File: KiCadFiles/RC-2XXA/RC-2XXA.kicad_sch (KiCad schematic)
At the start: 252 parts, among them J1 Conn_01x01_Pin, J2 Conn_01x04_Pin, J3 Conn_01x04_Pin, J4 Conn_01x07_Socket, J5 Conn_01x07_Socket, SW1 SW_DPST_x2, SW2 SW_DPST_x2, U1 TLV74318PDBVR, U2 PMW3360DM-T2QU, U3 TPD4E05U06DQAR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

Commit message: Add Solder Jumper component and associated wiring to RC-2XXA schematic
- Introduced a new Solder Jumper component (JP) with properties including reference, value, footprint, and description.
- Added multiple instances of the Solder Jumper at specified coordinates in the schematic.
- Updated wiring to accommodate the new component, ensuring proper connections.
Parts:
- added JP1, JP2, JP3: SolderJumper_2_Open, Jumper:SolderJumper-2_P1.3mm_Open_RoundedPad1.0x1.5mm, symbol Jumper:SolderJumper_2_Open
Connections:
- net CAPLED: now also JP2.1 (A); no longer R7.2
- net NUMLED: now also JP3.1 (A); no longer R9.2
- net SCLLED: now also JP1.1 (A); no longer R3.2
- new net: JP2.2 (B), R7.2
- new net: JP1.2 (B), R3.2
- new net: JP3.2 (B), R9.2
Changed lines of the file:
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@@
 	(wire
 		(pts
+			(xy 328.93 340.36) (xy 331.47 340.36)
+		)
+		(stroke
+			(width 0)
+			(type default)
+		)
+	)
+	(wire
+		(pts
 			(xy 204.47 24.13) (xy 204.47 34.29)
 		)
@@
 	(wire
 		(pts
+			(xy 328.93 370.84) (xy 331.47 370.84)
+		)
+		(stroke
+			(width 0)
+			(type default)
+		)
+	)
+	(wire
+		(pts
 			(xy 320.04 327.66) (xy 331.47 327.66)
 		)
@@
 	(wire
 		(pts
-			(xy 320.04 340.36) (xy 331.47 340.36)
+			(xy 320.04 340.36) (xy 321.31 340.36)
 		)
 		(stroke
@@
 	(wire
 		(pts
-			(xy 320.04 309.88) (xy 331.47 309.88)
+			(xy 320.04 309.88) (xy 322.58 309.88)
 		)
 		(stroke
@@
 	(wire
 		(pts
+			(xy 330.2 309.88) (xy 331.47 309.88)
+		)
+		(stroke
+			(width 0)
+			(type default)
+		)
+	)
+	(wire
+		(pts
 			(xy 351.79 107.95) (xy 361.95 107.95)
 		)
@@
 	(wire
 		(pts
-			(xy 320.04 370.84) (xy 331.47 370.84)
+			(xy 320.04 370.84) (xy 321.31 370.84)
 		)
 		(stroke
@@
 	)
 	(symbol
+		(lib_id "Jumper:SolderJumper_2_Open")
+		(at 326.39 309.88 0)
+		(unit 1)
+		(exclude_from_sim no)
+		(in_bom no)
+		(on_board yes)
+		(dnp no)
+		(property "Reference" "JP1"
+			(at 337.058 308.356 0)
+			(effects
+				(font
+					(size 1.27 1.27)
+				)
+			)
+		)
+		(property "Value" "SolderJumper_2_Open"
+			(at 326.39 306.07 0)
+			(effects
+				(font
+					(size 1.27 1.27)
+				)
+			)
+		)
+		(property "Footprint" "Jumper:SolderJumper-2_P1.3mm_Open_RoundedPad1.0x1.5mm"
+			(at 326.39 309.88 0)
+			(effects
+				(font
+					(size 1.27 1.27)
+				)
+				(hide yes)
+			)
+		)
+		(property "Datasheet" "~"
+			(at 326.39 309.88 0)
+			(effects
+				(font
+					(size 1.27 1.27)
+				)
+				(hide yes)
+			)
+		)
+		(property "Description" "Solder Jumper, 2-pole, open"
+			(at 326.39 309.88 0)
+			(effects
+				(font
+					(size 1.27 1.27)
+				)
+				(hide yes)
+			)
+		)
+		(pin "1"
+		)
+		(pin "2"
+		)
+		(instances
+			(project "RC-2XXA"
+				(path "/65196bbe-5350-405f-9fe2-667d33111e14"
+					(reference "JP1")
+					(unit 1)
+				)
+			)
+		)
+	)
+	(symbol
 		(lib_id "Device:D")
 		(at 487.68 66.04 90)
@@
 	)
 	(symbol
+		(lib_id "Jumper:SolderJumper_2_Open")
+		(at 325.12 370.84 0)
+		(unit 1)
+		(exclude_from_sim no)
+		(in_bom no)
+		(on_board yes)
+		(dnp no)
+		(property "Reference" "JP3"
+			(at 337.058 369.316 0)
+			(effects
+				(font
+					(size 1.27 1.27)
+				)
+			)
+		)
+		(property "Value" "SolderJumper_2_Open"
+			(at 325.12 367.03 0)
+			(effects
+				(font
+					(size 1.27 1.27)
+				)
+			)
+		)
+		(property "Footprint" "Jumper:SolderJumper-2_P1.3mm_Open_RoundedPad1.0x1.5mm"
+			(at 325.12 370.84 0)
+			(effects
+				(font
+					(size 1.27 1.27)
+				)
+				(hide yes)
+			)
+		)
+		(property "Datasheet" "~"
+			(at 325.12 370.84 0)
+			(effects
+				(font
+					(size 1.27 1.27)
+				)
+				(hide yes)
+			)
+		)
+		(property "Description" "Solder Jumper, 2-pole, open"
+			(at 325.12 370.84 0)
+			(effects
+				(font
+					(size 1.27 1.27)
+				)
+				(hide yes)
+			)
+		)
+		(pin "1"
+		)
+		(pin "2"
+		)
+		(instances
+			(project "RC-2XXA"
+				(path "/65196bbe-5350-405f-9fe2-667d33111e14"
+					(reference "JP3")
+					(unit 1)
+				)
+			)
+		)
+	)
+	(symbol
 		(lib_id "Device:C")
 		(at 149.86 388.62 0)
@@
 					(unit 1)
 				)
+			)
+		)
+	)
+	(symbol
+		(lib_id "Jumper:SolderJumper_2_Open")
+		(at 325.12 340.36 0)
+		(unit 1)
+		(exclude_from_sim no)
+		(in_bom no)
+		(on_board yes)
+		(dnp no)
+		(property "Reference" "JP2"
+			(at 337.058 338.836 0)
+			(effects
+				(font
+					(size 1.27 1.27)
+				)
+			)
+		)
+		(property "Value" "SolderJumper_2_Open"
+			(at 325.12 336.55 0)
+			(effects
+				(font
+					(size 1.27 1.27)
+				)
+			)
+		)
+		(property "Footprint" "Jumper:SolderJumper-2_P1.3mm_Open_RoundedPad1.0x1.5mm"
+			(at 325.12 340.36 0)
+			(effects
+				(font
+					(size 1.27 1.27)
+				)
+				(hide yes)
+			)
+		)
+		(property "Datasheet" "~"
+			(at 325.12 340.36 0)
+			(effects
+				(font
+					(size 1.27 1.27)
+				)
+				(hide yes)
+			)
+		)
+		(property "Description" "Solder Jumper, 2-pole, open"
+			(at 325.12 340.36 0)
+			(effects
+				(font
+					(size 1.27 1.27)
+				)
+				(hide yes)
+			)
+		)
+		(pin "1"
+		)
+		(pin "2"
+		)
+		(instances
+			(project "RC-2XXA"
+				(path "/65196bbe-5350-405f-9fe2-667d33111e14"
+					(reference "JP2")
+					(unit 1)
+				)

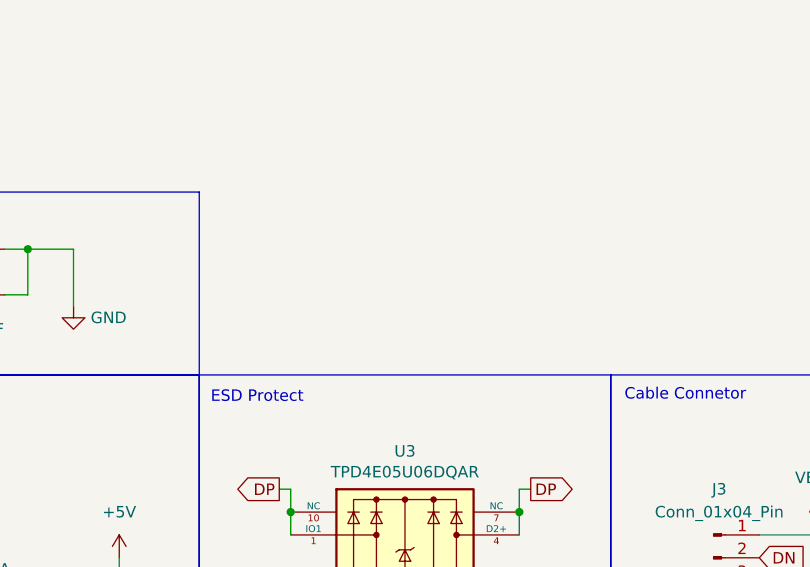
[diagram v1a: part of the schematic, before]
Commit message: Add Mounting Hole Pad and GND symbol to schematic
- Introduced a new symbol for a mounting hole pad with properties including reference, value, footprint, and description.
- Added a graphical representation of the mounting hole pad with a circle.
- Included a GND symbol with properties for reference, value, and description, creating a global label for ground.
- Updated the schematic layout to accommodate the new components.
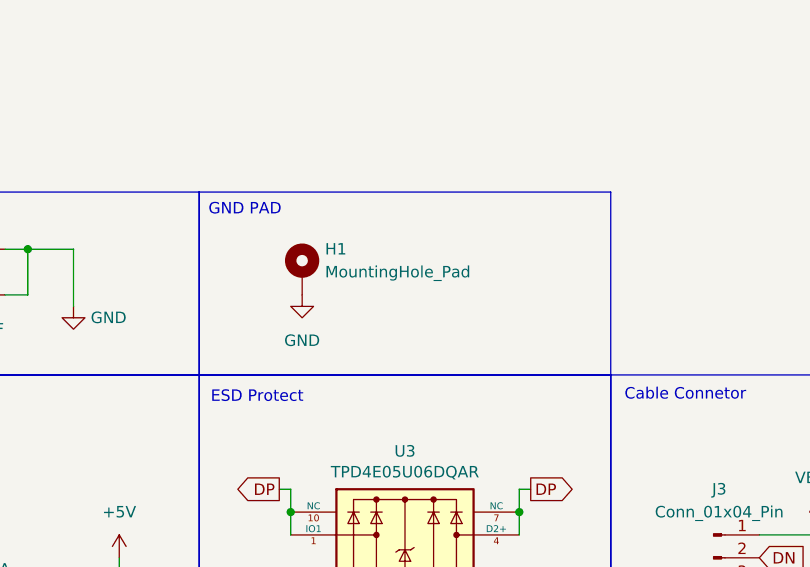
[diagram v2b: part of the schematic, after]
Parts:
- added H1: MountingHole_Pad, My-Fi Footprints:Cherry-GND-PAD, symbol Mechanical:MountingHole_Pad
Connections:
- net GND: now also H1.1
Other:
- note added: "GND PAD"
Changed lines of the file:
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@@
 	)
 	(rectangle
+		(start 176.53 303.53)
+		(end 222.25 323.85)
+		(stroke
+			(width 0)
+			(type default)
+		)
+		(fill
+			(type none)
+		)
+	)
+	(rectangle
 		(start 127 303.53)
 		(end 176.53 323.85)
@@
 		)
 	)
+	(text "GND PAD"
+		(exclude_from_sim no)
+		(at 177.546 305.562 0)
+		(effects
+			(font
+				(size 1.27 1.27)
+			)
+			(justify left)
+		)
+	)
 	(junction
 		(at 204.47 102.87)
@@
 	)
 	(symbol
+		(lib_id "Mechanical:MountingHole_Pad")
+		(at 187.96 312.42 0)
+		(unit 1)
+		(exclude_from_sim no)
+		(in_bom no)
+		(on_board yes)
+		(dnp no)
+		(fields_autoplaced yes)
+		(property "Reference" "H1"
+			(at 190.5 309.8799 0)
+			(effects
+				(font
+					(size 1.27 1.27)
+				)
+				(justify left)
+			)
+		)
+		(property "Value" "MountingHole_Pad"
+			(at 190.5 312.4199 0)
+			(effects
+				(font
+					(size 1.27 1.27)
+				)
+				(justify left)
+			)
+		)
+		(property "Footprint" "My-Fi Footprints:Cherry-GND-PAD"
+			(at 187.96 312.42 0)
+			(effects
+				(font
+					(size 1.27 1.27)
+				)
+				(hide yes)
+			)
+		)
+		(property "Datasheet" "~"
+			(at 187.96 312.42 0)
+			(effects
+				(font
+					(size 1.27 1.27)
+				)
+				(hide yes)
+			)
+		)
+		(property "Description" "Mounting Hole with connection"
+			(at 187.96 312.42 0)
+			(effects
+				(font
+					(size 1.27 1.27)
+				)
+				(hide yes)
+			)
+		)
+		(pin "1"
+		)
+		(instances
+			(project ""
+				(path "/65196bbe-5350-405f-9fe2-667d33111e14"
+					(reference "H1")
+					(unit 1)
+				)
+			)
+		)
+	)
+	(symbol
 		(lib_id "Regulator_Linear:XC6206PxxxMR")
 		(at 232.41 384.81 0)
@@
 					(unit 1)
 				)
+			)
+		)
+	)
+	(symbol
+		(lib_id "power:GND")
+		(at 187.96 314.96 0)
+		(unit 1)
+		(exclude_from_sim no)
+		(in_bom yes)
+		(on_board yes)
+		(dnp no)
+		(fields_autoplaced yes)
+		(property "Reference" "#PWR014"
+			(at 187.96 321.31 0)
+			(effects
+				(font
+					(size 1.27 1.27)
+				)
+				(hide yes)
+			)
+		)
+		(property "Value" "GND"
+			(at 187.96 320.04 0)
+			(effects
+				(font
+					(size 1.27 1.27)
+				)
+			)
+		)
+		(property "Footprint" ""
+			(at 187.96 314.96 0)
+			(effects
+				(font
+					(size 1.27 1.27)
+				)
+				(hide yes)
+			)
+		)
+		(property "Datasheet" ""
+			(at 187.96 314.96 0)
+			(effects
+				(font
+					(size 1.27 1.27)
+				)
+				(hide yes)
+			)
+		)
+		(property "Description" "Power symbol creates a global label with name \"GND\" , ground"
+			(at 187.96 314.96 0)
+			(effects
+				(font
+					(size 1.27 1.27)
+				)
+				(hide yes)
+			)
+		)
+		(pin "1"
+		)
+		(instances
+			(project "RC-2XXA"
+				(path "/65196bbe-5350-405f-9fe2-667d33111e14"
+					(reference "#PWR014")
+					(unit 1)
+				)

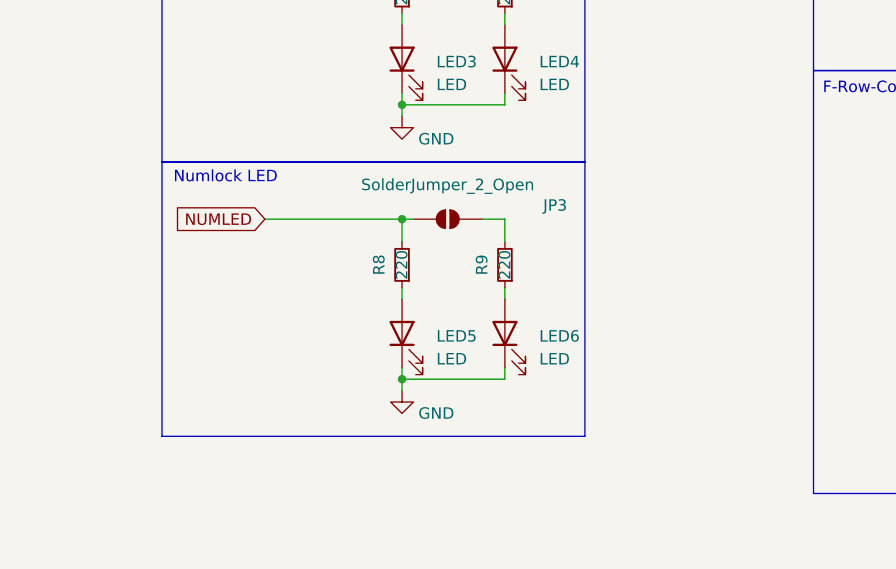
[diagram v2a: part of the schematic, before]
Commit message: Add Solder Jumper and update component positions in schematic
- Introduced a new Solder Jumper component (JP4) with properties and graphical representation.
- Adjusted positions of several components including resistors (R8, R9, R11) and LEDs (LED6, LED7) for better layout.
- Updated junctions and wire connections to reflect new component placements.
- Removed redundant junctions and wires to clean up the schematic.
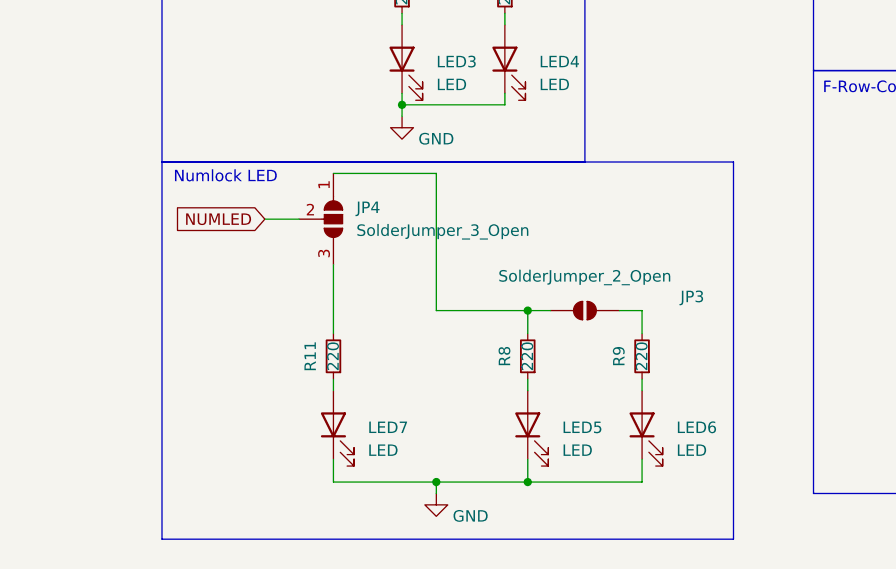
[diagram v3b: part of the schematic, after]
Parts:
- added JP4: SolderJumper_3_Open, Jumper:SolderJumper-3_P1.3mm_Open_RoundedPad1.0x1.5mm, symbol Jumper:SolderJumper_3_Open
- added LED7: LED, My-Fi Footprints:DIP_LED_MX_3mm, symbol Device:LED
- added R11: 220, Resistor_SMD:R_0805_2012Metric_Pad1.20x1.40mm_HandSolder, symbol Device:R_Small
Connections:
- net GND: now also LED7.1 (K)
- net NUMLED: now also JP4.2 (C); no longer JP3.1 (A), R8.2
- new net: JP3.1 (A), JP4.1 (A), R8.2
- new net: JP4.3 (B), R11.2
- new net: LED7.2 (A), R11.1
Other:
- moved on the sheet: JP3, LED5, LED6, R8, R9

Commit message: Refactor code structure for improved readability and maintainability
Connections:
- net COL0: now also U4.43 (PB7)
- net COL1: now also U4.42 (PB6)
- net COL10: now also U4.28 (PB15)
- net COL11: now also U4.27 (PB14)
- net COL12: now also U4.26 (PB13)
- net COL13: now also U4.25 (PB12)
- net COL14: now also U4.22 (PB11)
- net COL15: now also U4.21 (PB10)
- net COL16: now also U4.20 (PB2)
- net COL17: now also U4.5 (PF0)
- net COL18: now also U4.4 (PC15)
- net COL19: now also U4.3 (PC14)
- net COL2: now also U4.40 (PB4)
- net COL20: now also U4.2 (PC13)
- net COL3: now also U4.39 (PB3)
- net COL4: now also U4.38 (PA15)
- net COL5: now also U4.37 (PA14)
- net COL6: now also U4.34 (PA13)
- net COL7: now also U4.31 (PA10)
- net COL8: now also U4.30 (PA9)
- net COL9: now also U4.29 (PA8)
- net NUMLED: now also JP3.1 (A)
- net ROW0: now also U4.45 (PB8)
- net ROW1: now also U4.46 (PB9)
- net ROW2: now also U4.13 (PA3)
- net ROW3: now also U4.12 (PA2)
- net ROW4: now also U4.11 (PA1)
- net ROW5: now also U4.10 (PA0)
- net ROW6: now also U4.6 (PF1)
- net at JP4.1 (A), R8.2: no longer JP3.1 (A)
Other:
- moved on the sheet: JP4

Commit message: Refactor code structure for improved readability and maintainability
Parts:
- removed J4: Conn_01x07_Socket, Connector_JST:JST_SH_SM07B-SRSS-TB_1x07-1MP_P1.00mm_Horizontal, symbol Connector:Conn_01x07_Socket
- added J4: Conn_01x08_Socket, Connector_JST:JST_SH_SM08B-SRSS-TB_1x08-1MP_P1.00mm_Horizontal, symbol Connector:Conn_01x08_Socket
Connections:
- net COL0: now also J4.5 (Pin_5)
- net COL1: now also J4.4 (Pin_4)
- net COL2: now also J4.3 (Pin_3)
- net COL3: now also J4.2 (Pin_2)
- net COL4: now also J4.1 (Pin_1)
- net GND: now also J4.8 (Pin_8)
- net ROW0: now also J4.7 (Pin_7)
- net ROW1: now also J4.6 (Pin_6)
